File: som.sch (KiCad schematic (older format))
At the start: 31 parts, among them M1 SC606T

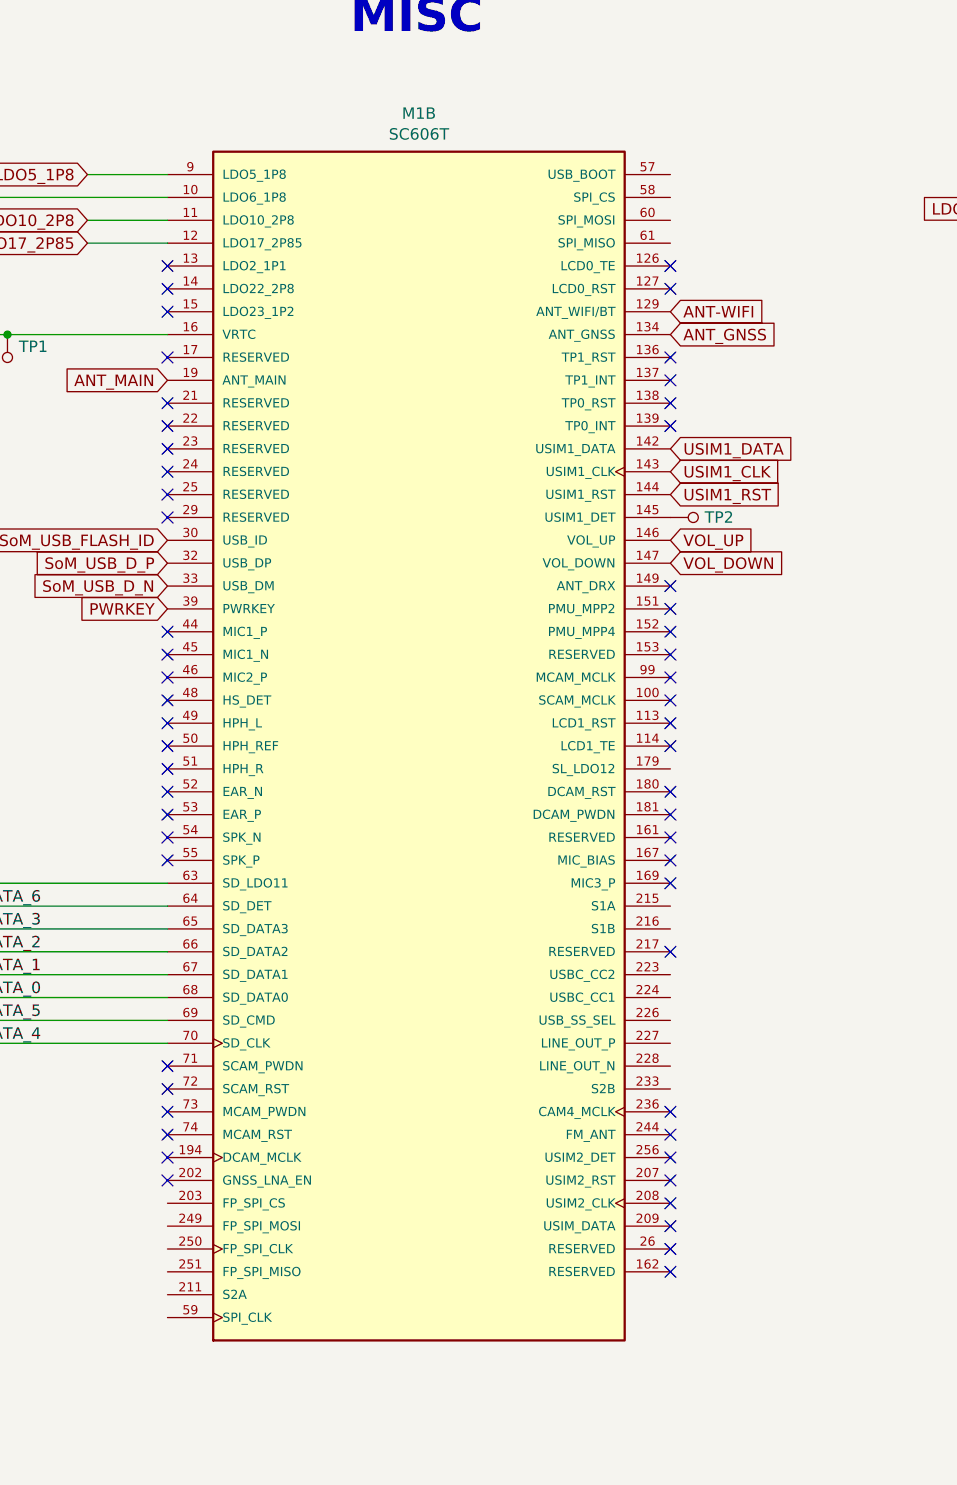
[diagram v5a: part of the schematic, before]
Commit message: Added USB BOOT, placed USR LEDs and buttons, connected Test Points
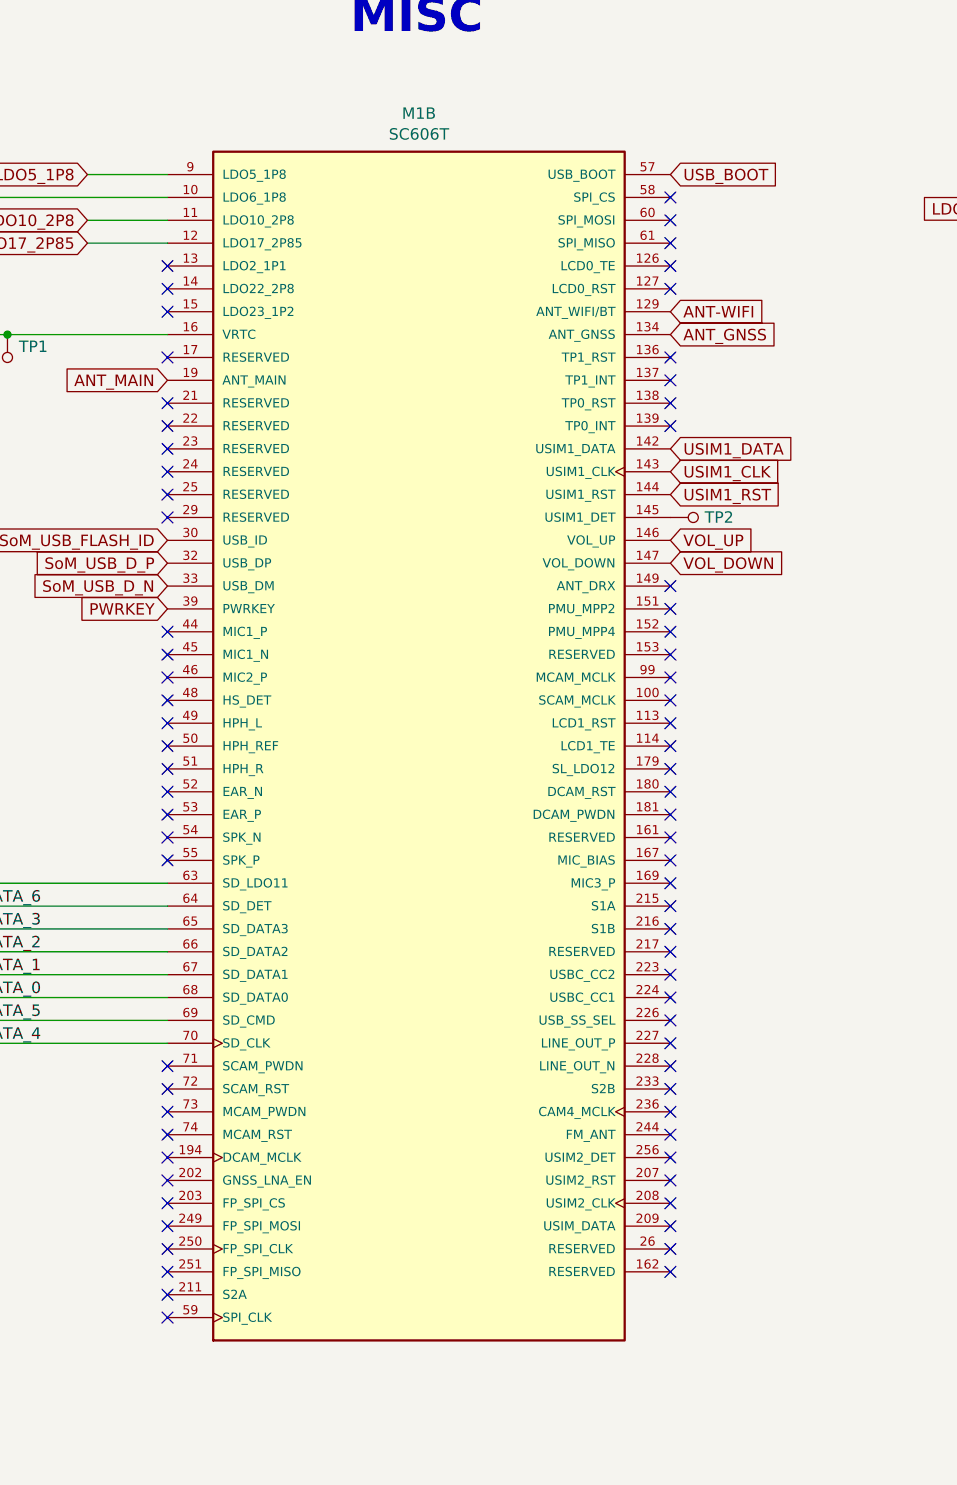
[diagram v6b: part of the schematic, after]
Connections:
- net USB_BOOT: now reaches M1.57 (USB_BOOT)
- no-connect marks 93 -> 111
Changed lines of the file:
@@
 Text GLabel 14550 2700 2    50   Input ~ 0
 SoMtoDisplay_CLK_N
+NoConn ~ 5000 1750
+NoConn ~ 5000 1850
+NoConn ~ 5000 1950
+NoConn ~ 5000 4250
+Text GLabel 5000 1650 2    50   Input ~ 0
+USB_BOOT
+NoConn ~ 5000 4850
+NoConn ~ 5000 4950
+NoConn ~ 5000 5150
+NoConn ~ 5000 5250
+NoConn ~ 5000 5350
+NoConn ~ 5000 5450
+NoConn ~ 5000 5550
+NoConn ~ 5000 5650
+NoConn ~ 2800 6550
+NoConn ~ 2800 6650
+NoConn ~ 2800 6350
+NoConn ~ 2800 6250
+NoConn ~ 2800 6150
+NoConn ~ 2800 6450
 Wire Bus Line
 	1750 4650 1750 5350

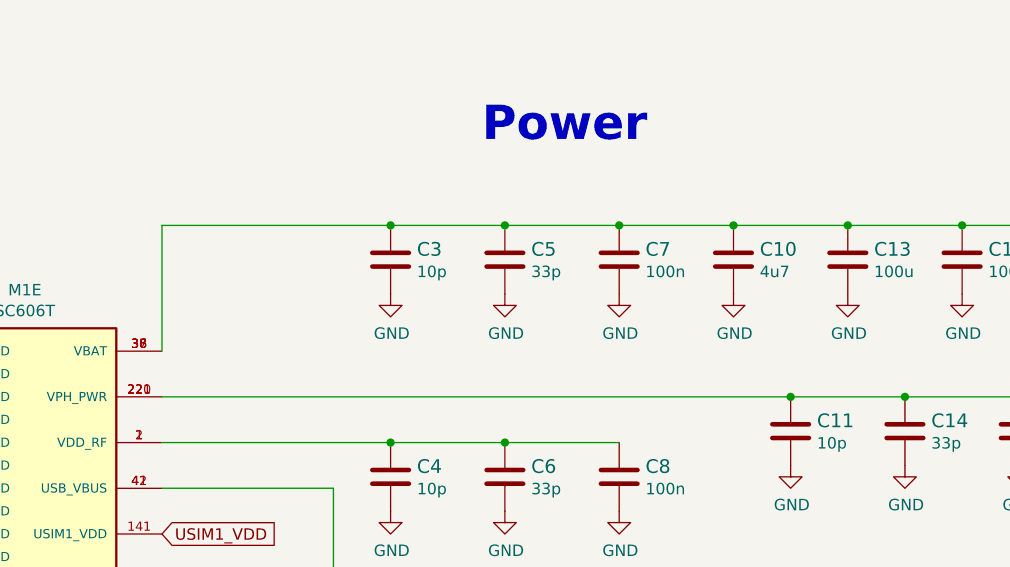
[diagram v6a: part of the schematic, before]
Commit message: Started rearrangement of components. USB connectors changed to 2xUSB-C
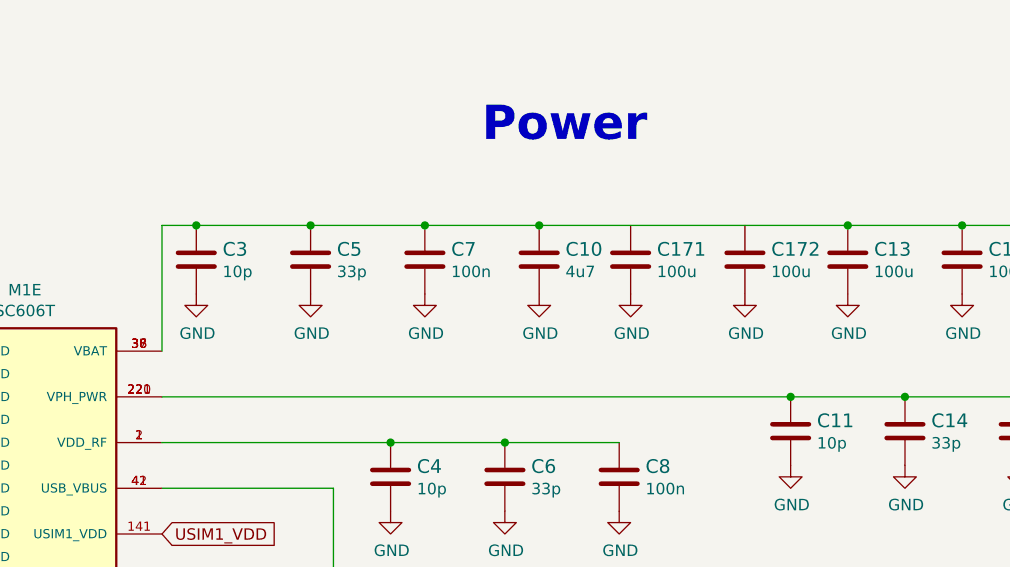
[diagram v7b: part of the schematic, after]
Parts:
- added C171, C172: C_100u_1206, sc606-baseboard-footprints:1206-cap, symbol sc606-baseboard:C_100u_1206
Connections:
- net GND: now also C171.2, C172.2
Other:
- moved on the sheet: C10, C3, C5, C7
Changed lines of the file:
@@
 L sc606-baseboard:C_10p_0402 C3
 U 1 1 61FCFAC1
-P 3000 8150
-F 0 "C3" H 3115 8195 60  0000 L CNN
-F 1 "C_10p_0402" H 3000 8000 60  0001 C CNN
-F 2 "sc606-baseboard-footprints:0402-cap" H 3200 8350 60  0001 L CNN
-F 3 "" H 3000 8150 50  0001 C CNN
-F 4 "MULTICOMP" H 3200 8550 60  0001 L CNN "Manufacturer"
-F 5 "MC0402N100D500CT" H 3200 8450 60  0001 L CNN "MPN"
-F 6 "10p" H 3115 8097 50  0000 L CNN "Val"
-	1    3000 8150
+P 2150 8150
+F 0 "C3" H 2265 8195 60  0000 L CNN
+F 1 "C_10p_0402" H 2150 8000 60  0001 C CNN
+F 2 "sc606-baseboard-footprints:0402-cap" H 2350 8350 60  0001 L CNN
+F 3 "" H 2150 8150 50  0001 C CNN
+F 4 "MULTICOMP" H 2350 8550 60  0001 L CNN "Manufacturer"
+F 5 "MC0402N100D500CT" H 2350 8450 60  0001 L CNN "MPN"
+F 6 "10p" H 2265 8097 50  0000 L CNN "Val"
+	1    2150 8150
 	1    0    0    -1
 $EndComp
@@
 L sc606-baseboard:C_33p_0402 C5
 U 1 1 61FD10EC
-P 3500 8150
-F 0 "C5" H 3615 8195 60  0000 L CNN
-F 1 "C_33p_0402" H 3500 8000 60  0001 C CNN
-F 2 "sc606-baseboard-footprints:0402-cap" H 3700 8350 60  0001 L CNN
-F 3 "" H 3500 8150 50  0001 C CNN
-F 4 "MULTICOMP" H 3700 8550 60  0001 L CNN "Manufacturer"
-F 5 "MC0402N330J500CT" H 3700 8450 60  0001 L CNN "MPN"
-F 6 "33p" H 3615 8097 50  0000 L CNN "Val"
-	1    3500 8150
+P 2650 8150
+F 0 "C5" H 2765 8195 60  0000 L CNN
+F 1 "C_33p_0402" H 2650 8000 60  0001 C CNN
+F 2 "sc606-baseboard-footprints:0402-cap" H 2850 8350 60  0001 L CNN
+F 3 "" H 2650 8150 50  0001 C CNN
+F 4 "MULTICOMP" H 2850 8550 60  0001 L CNN "Manufacturer"
+F 5 "MC0402N330J500CT" H 2850 8450 60  0001 L CNN "MPN"
+F 6 "33p" H 2765 8097 50  0000 L CNN "Val"
+	1    2650 8150
 	1    0    0    -1
 $EndComp
@@
 L sc606-baseboard:C_100n_0402 C7
 U 1 1 61FD2DBE
-P 4000 8150
-F 0 "C7" H 4115 8195 60  0000 L CNN
-F 1 "C_100n_0402" H 4000 8000 60  0001 C CNN
-F 2 "sc606-baseboard-footprints:0402-cap" H 4200 8350 60  0001 L CNN
-F 3 "" H 4000 8150 50  0001 C CNN
-F 4 "Walsin" H 4200 8550 60  0001 L CNN "Manufacturer"
-F 5 "0402X104K6R3CT" H 4200 8450 60  0001 L CNN "MPN"
-F 6 "100n" H 4115 8097 50  0000 L CNN "Val"
-	1    4000 8150
+P 3150 8150
+F 0 "C7" H 3265 8195 60  0000 L CNN
+F 1 "C_100n_0402" H 3150 8000 60  0001 C CNN
+F 2 "sc606-baseboard-footprints:0402-cap" H 3350 8350 60  0001 L CNN
+F 3 "" H 3150 8150 50  0001 C CNN
+F 4 "Walsin" H 3350 8550 60  0001 L CNN "Manufacturer"
+F 5 "0402X104K6R3CT" H 3350 8450 60  0001 L CNN "MPN"
+F 6 "100n" H 3265 8097 50  0000 L CNN "Val"
+	1    3150 8150
 	1    0    0    -1
 $EndComp
@@
 L sc606-baseboard:C_4u7_0402 C10
 U 1 1 61FD43E8
-P 4500 8150
-F 0 "C10" H 4615 8195 60  0000 L CNN
-F 1 "C_4u7_0402" H 4500 8000 60  0001 C CNN
-F 2 "sc606-baseboard-footprints:0402-cap" H 4700 8350 60  0001 L CNN
-F 3 "" H 4500 8150 50  0001 C CNN
-F 4 "MURATA" H 4700 8550 60  0001 L CNN "Manufacturer"
-F 5 "GRM155R61A475MEAAD" H 4700 8450 60  0001 L CNN "MPN"
-F 6 "4u7" H 4615 8097 50  0000 L CNN "Val"
-	1    4500 8150
+P 3650 8150
+F 0 "C10" H 3765 8195 60  0000 L CNN
+F 1 "C_4u7_0402" H 3650 8000 60  0001 C CNN
+F 2 "sc606-baseboard-footprints:0402-cap" H 3850 8350 60  0001 L CNN
+F 3 "" H 3650 8150 50  0001 C CNN
+F 4 "MURATA" H 3850 8550 60  0001 L CNN "Manufacturer"
+F 5 "GRM155R61A475MEAAD" H 3850 8450 60  0001 L CNN "MPN"
+F 6 "4u7" H 3765 8097 50  0000 L CNN "Val"
+	1    3650 8150
 	1    0    0    -1
 $EndComp
@@
 Wire Wire Line
 	2000 8000 2000 8550
-Connection ~ 3000 8000
-Wire Wire Line
-	3000 8000 2000 8000
-Connection ~ 3500 8000
-Wire Wire Line
-	3500 8000 3000 8000
-Connection ~ 4000 8000
-Wire Wire Line
-	4000 8000 3500 8000
-Connection ~ 4500 8000
-Wire Wire Line
-	4500 8000 4000 8000
 Connection ~ 5000 8000
-Wire Wire Line
-	5000 8000 4500 8000
 Connection ~ 5500 8000
 Wire Wire Line
@@
 L sc606-baseboard:GND #PWR03
 U 1 1 62062730
-P 3000 8300
-F 0 "#PWR03" H 3000 8050 50  0001 C CNN
-F 1 "GND" H 3005 8127 50  0000 C CNN
-F 2 "" H 3000 8300 50  0001 C CNN
-F 3 "" H 3000 8300 50  0001 C CNN
-	1    3000 8300
+P 2150 8300
+F 0 "#PWR03" H 2150 8050 50  0001 C CNN
+F 1 "GND" H 2155 8127 50  0000 C CNN
+F 2 "" H 2150 8300 50  0001 C CNN
+F 3 "" H 2150 8300 50  0001 C CNN
+	1    2150 8300
 	1    0    0    -1
 $EndComp
@@
 L sc606-baseboard:GND #PWR05
 U 1 1 62063329
-P 3500 8300
-F 0 "#PWR05" H 3500 8050 50  0001 C CNN
-F 1 "GND" H 3505 8127 50  0000 C CNN
-F 2 "" H 3500 8300 50  0001 C CNN
-F 3 "" H 3500 8300 50  0001 C CNN
-	1    3500 8300
+P 2650 8300
+F 0 "#PWR05" H 2650 8050 50  0001 C CNN
+F 1 "GND" H 2655 8127 50  0000 C CNN
+F 2 "" H 2650 8300 50  0001 C CNN
+F 3 "" H 2650 8300 50  0001 C CNN
+	1    2650 8300
 	1    0    0    -1
 $EndComp
@@
 L sc606-baseboard:GND #PWR07
 U 1 1 62064072
-P 4000 8300
-F 0 "#PWR07" H 4000 8050 50  0001 C CNN
-F 1 "GND" H 4005 8127 50  0000 C CNN
-F 2 "" H 4000 8300 50  0001 C CNN
-F 3 "" H 4000 8300 50  0001 C CNN
-	1    4000 8300
+P 3150 8300
+F 0 "#PWR07" H 3150 8050 50  0001 C CNN
+F 1 "GND" H 3155 8127 50  0000 C CNN
+F 2 "" H 3150 8300 50  0001 C CNN
+F 3 "" H 3150 8300 50  0001 C CNN
+	1    3150 8300
 	1    0    0    -1
 $EndComp
@@
 L sc606-baseboard:GND #PWR010
 U 1 1 62065256
-P 4500 8300
-F 0 "#PWR010" H 4500 8050 50  0001 C CNN
-F 1 "GND" H 4505 8127 50  0000 C CNN
-F 2 "" H 4500 8300 50  0001 C CNN
-F 3 "" H 4500 8300 50  0001 C CNN
-	1    4500 8300
+P 3650 8300
+F 0 "#PWR010" H 3650 8050 50  0001 C CNN
+F 1 "GND" H 3655 8127 50  0000 C CNN
+F 2 "" H 3650 8300 50  0001 C CNN
+F 3 "" H 3650 8300 50  0001 C CNN
+	1    3650 8300
 	1    0    0    -1
 $EndComp
@@
 NoConn ~ 2800 6150
 NoConn ~ 2800 6450
+Connection ~ 2150 8000
+Wire Wire Line
+	2150 8000 2000 8000
+Connection ~ 2650 8000
+Wire Wire Line
+	2650 8000 2150 8000
+Connection ~ 3150 8000
+Connection ~ 3650 8000
+Wire Wire Line
+	2650 8000 3150 8000
+Wire Wire Line
+	3150 8000 3650 8000
+Wire Wire Line
+	3650 8000 5000 8000
+$Comp
+L sc606-baseboard:C_100u_1206 C171
+U 1 1 627F7180
+P 4050 8150
+F 0 "C171" H 4165 8195 60  0000 L CNN
+F 1 "C_100u_1206" H 4050 8000 60  0001 C CNN
+F 2 "sc606-baseboard-footprints:1206-cap" H 4250 8350 60  0001 L CNN
+F 3 "" H 4050 8150 50  0001 C CNN
+F 4 "Vishay" H 4250 8550 60  0001 L CNN "Manufacturer"
+F 5 "TMCMA0J107MTRF" H 4250 8450 60  0001 L CNN "MPN"
+F 6 "100u" H 4165 8097 50  0000 L CNN "Val"
+	1    4050 8150
+	1    0    0    -1
+$EndComp
+$Comp
+L sc606-baseboard:GND #PWR0170
+U 1 1 627F7186
+P 4050 8300
+F 0 "#PWR0170" H 4050 8050 50  0001 C CNN
+F 1 "GND" H 4055 8127 50  0000 C CNN
+F 2 "" H 4050 8300 50  0001 C CNN
+F 3 "" H 4050 8300 50  0001 C CNN
+	1    4050 8300
+	1    0    0    -1
+$EndComp
+$Comp
+L sc606-baseboard:C_100u_1206 C172
+U 1 1 627FB1E9
+P 4550 8150
+F 0 "C172" H 4665 8195 60  0000 L CNN
+F 1 "C_100u_1206" H 4550 8000 60  0001 C CNN
+F 2 "sc606-baseboard-footprints:1206-cap" H 4750 8350 60  0001 L CNN
+F 3 "" H 4550 8150 50  0001 C CNN
+F 4 "Vishay" H 4750 8550 60  0001 L CNN "Manufacturer"
+F 5 "TMCMA0J107MTRF" H 4750 8450 60  0001 L CNN "MPN"
+F 6 "100u" H 4665 8097 50  0000 L CNN "Val"
+	1    4550 8150
+	1    0    0    -1
+$EndComp
+$Comp
+L sc606-baseboard:GND #PWR0171
+U 1 1 627FB1EF
+P 4550 8300
+F 0 "#PWR0171" H 4550 8050 50  0001 C CNN
+F 1 "GND" H 4555 8127 50  0000 C CNN
+F 2 "" H 4550 8300 50  0001 C CNN
+F 3 "" H 4550 8300 50  0001 C CNN
+	1    4550 8300
+	1    0    0    -1
+$EndComp
 Wire Bus Line
 	1750 4650 1750 5350

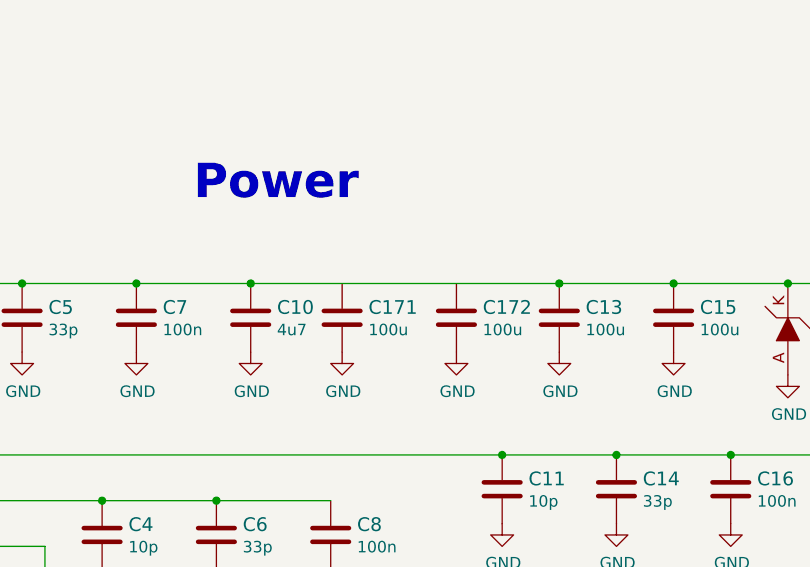
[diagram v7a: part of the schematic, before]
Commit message: All components placed on board
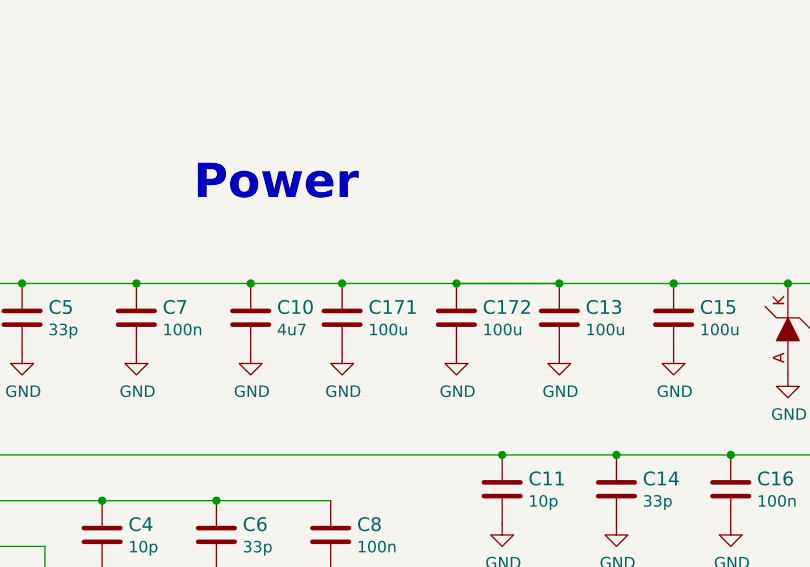
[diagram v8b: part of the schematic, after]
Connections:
- net V_SOM: now also C171.1, C172.1
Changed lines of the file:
@@
 Wire Wire Line
 	3150 8000 3650 8000
-Wire Wire Line
-	3650 8000 5000 8000
 $Comp
 L sc606-baseboard:C_100u_1206 C171
@@
 	1    0    0    -1
 $EndComp
+Wire Wire Line
+	3650 8000 4050 8000
+Connection ~ 4050 8000
+Wire Wire Line
+	4050 8000 4550 8000
+Wire Wire Line
+	4550 8000 5000 8000
 Wire Bus Line
 	1750 4650 1750 5350
+Connection ~ 4550 8000
+Wire Wire Line
+	4550 8000 5000 8000
 $EndSCHEMATC
